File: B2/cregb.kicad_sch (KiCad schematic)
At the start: 9 parts, among them U105 74HC244, U108 74HC32, U110 74HC04, U115 74HC74, U120 74HC74, U124 74HC00, U125 74HC74, U127 74HC08, U128 74HC377

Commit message: B2 almost ready
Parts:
- removed U115, U120: 74HC74, Package_SO:SO-14_3.9x8.65mm_P1.27mm, symbol 74xx:74HC74
- added U316, U999: 74HC74, Package_SO:SO-14_3.9x8.65mm_P1.27mm, symbol 74xx:74HC74
- renumbered U105 to U205, U110 to U302, U124 to U303, U108 to U304, U128 to U305, U127 to U306, U125 to U308
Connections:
- net PHI2: now also U316.11 (C), U999.11 (C)
- net VCC: now also U316.10 (~{S}), U316.13 (~{R}), U999.1 (~{R}), U999.10 (~{S}), U999.13 (~{R}), U999.4 (~{S})
- net ~{PHI2}: now also U999.3 (C)
- net TBRUNMODE: now reaches U304.10
- net TBRUNMODE: now also U205.15 (2A1), U305.12 (Q4), U316.12 (D)
- net at U308.9 (Q): now also U999.12 (D)
- net PB6ON renamed PB7ON
- net SPMODE renamed TBINMODE1
- net TAINMODE renamed TBINMODE0
- net TAOUTMODE renamed TBOUTMODE
- removed net TARUNMODE: U205.15 (2A1), U304.9, U305.12 (Q4)
- net TAUNDERFLOW renamed TBUNDERFLOW
- net TODIN renamed ALARM
- net rTASTART renamed rTBSTART
- net rTBSTART: now also U999.2 (D)
- net ~{EN14} renamed ~{EN15}
- new net: U304.9, U316.9 (Q)
- new net TBLOAD: U999.9 (Q)
- new net TBSTART: U999.5 (Q)
- new net ~{TBSTART}: U999.6 (~{Q})
- no-connect marks 7 -> 6
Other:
- moved on the sheet: U304C

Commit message: Almost 0.1.1
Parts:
- renumbered U304 to U208, U302 to U210, U316 to U213, U999 to U222, U308 to U223, U303 to U227, U305 to U228, U306 to U229
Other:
- title: 74HCT6526 Board 1 -> 74HCT6526 Board 2
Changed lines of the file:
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@@
   (paper "A4")
   (title_block
-    (title "74HCT6526 Board 1")
-    (date "2022-03-20")
-    (rev "0.0")
+    (title "74HCT6526 Board 2")
+    (date "2022-08-17")
+    (rev "0.1")
     (company "Daniel Molina")
     (comment 1 "https://github.com/dmolinagarcia/74HCT6526")
@@
   (symbol (lib_id "74xx:74HC04") (at 87.63 102.87 0) (unit 5)
     (in_bom yes) (on_board yes)
-    (property "Reference" "U302" (id 0) (at 86.995 102.87 0))
+    (property "Reference" "U210" (id 0) (at 86.995 102.87 0))
     (property "Value" "74HC04" (id 1) (at 87.63 97.8686 0))
     (property "Footprint" "Package_SO:SOIC-14_3.9x8.7mm_P1.27mm" (id 2) (at 87.63 102.87 0)
@@
   (symbol (lib_id "74xx:74HC00") (at 50.8 68.58 0) (unit 1)
     (in_bom yes) (on_board yes)
-    (property "Reference" "U303" (id 0) (at 50.8 68.58 0))
+    (property "Reference" "U227" (id 0) (at 50.8 68.58 0))
     (property "Value" "74HC00" (id 1) (at 50.8 74.93 0))
     (property "Footprint" "Package_SO:SOIC-14_3.9x8.7mm_P1.27mm" (id 2) (at 50.8 68.58 0)
@@
   (symbol (lib_id "74xx:74HC74") (at 127 116.84 0) (unit 2)
     (in_bom yes) (on_board yes) (fields_autoplaced)
-    (property "Reference" "U316" (id 0) (at 129.0194 107.7935 0)
+    (property "Reference" "U213" (id 0) (at 129.0194 107.7935 0)
       (effects (font (size 1.27 1.27)) (justify left))
     )
@@
   (symbol (lib_id "74xx:74LS32") (at 153.67 116.84 0) (unit 3)
     (in_bom yes) (on_board yes)
-    (property "Reference" "U304" (id 0) (at 153.67 116.84 0))
+    (property "Reference" "U208" (id 0) (at 153.67 116.84 0))
     (property "Value" "74HC32" (id 1) (at 153.035 122.555 0))
     (property "Footprint" "Package_SO:SOIC-14_3.9x8.7mm_P1.27mm" (id 2) (at 153.67 116.84 0)
@@
   (symbol (lib_id "74xx:74HC00") (at 171.45 119.38 0) (unit 2)
     (in_bom yes) (on_board yes)
-    (property "Reference" "U303" (id 0) (at 171.45 119.38 0))
+    (property "Reference" "U227" (id 0) (at 171.45 119.38 0))
     (property "Value" "74HC00" (id 1) (at 171.45 114.3786 0))
     (property "Footprint" "Package_SO:SOIC-14_3.9x8.7mm_P1.27mm" (id 2) (at 171.45 119.38 0)
@@
   (symbol (lib_id "74xx:74HC74") (at 127 142.24 0) (unit 2)
     (in_bom yes) (on_board yes)
-    (property "Reference" "U308" (id 0) (at 126.365 142.24 0)
+    (property "Reference" "U223" (id 0) (at 126.365 142.24 0)
       (effects (font (size 1.27 1.27)) (justify left))
     )
@@
   (symbol (lib_id "74xx:74HC74") (at 160.02 142.24 0) (unit 2)
     (in_bom yes) (on_board yes)
-    (property "Reference" "U999" (id 0) (at 158.75 143.51 0)
+    (property "Reference" "U222" (id 0) (at 158.75 143.51 0)
       (effects (font (size 1.27 1.27)) (justify left))
     )
@@
   (symbol (lib_id "74xx:74HC74") (at 226.06 110.49 0) (unit 1)
     (in_bom yes) (on_board yes)
-    (property "Reference" "U999" (id 0) (at 224.79 110.49 0)
+    (property "Reference" "U222" (id 0) (at 224.79 110.49 0)
       (effects (font (size 1.27 1.27)) (justify left))
     )
@@
   (symbol (lib_id "74xx:74HC74") (at 180.34 95.25 0) (unit 1)
     (in_bom yes) (on_board yes)
-    (property "Reference" "U308" (id 0) (at 179.07 95.25 0)
+    (property "Reference" "U223" (id 0) (at 179.07 95.25 0)
       (effects (font (size 1.27 1.27)) (justify left))
     )
@@
   (symbol (lib_id "Custom 74xx:74HC08") (at 107.95 105.41 0) (unit 1)
     (in_bom yes) (on_board yes)
-    (property "Reference" "U306" (id 0) (at 107.315 105.41 0))
+    (property "Reference" "U229" (id 0) (at 107.315 105.41 0))
     (property "Value" "74HC08" (id 1) (at 107.95 100.4086 0))
     (property "Footprint" "Package_SO:SO-14_3.9x8.65mm_P1.27mm" (id 2) (at 107.95 105.41 0)
@@
   (symbol (lib_id "74xx:74LS32") (at 55.88 80.01 0) (unit 4)
     (in_bom yes) (on_board yes)
-    (property "Reference" "U304" (id 0) (at 55.88 80.01 0))
+    (property "Reference" "U208" (id 0) (at 55.88 80.01 0))
     (property "Value" "74HC32" (id 1) (at 55.88 85.09 0))
     (property "Footprint" "Package_SO:SOIC-14_3.9x8.7mm_P1.27mm" (id 2) (at 55.88 80.01 0)
@@
   (symbol (lib_id "74xx:74LS377") (at 100.33 46.99 0) (unit 1)
     (in_bom yes) (on_board yes) (fields_autoplaced)
-    (property "Reference" "U305" (id 0) (at 102.3494 27.7835 0)
+    (property "Reference" "U228" (id 0) (at 102.3494 27.7835 0)
       (effects (font (size 1.27 1.27)) (justify left))
     )
@@
   (symbol (lib_id "74xx:74HC00") (at 67.31 66.04 0) (unit 4)
     (in_bom yes) (on_board yes)
-    (property "Reference" "U303" (id 0) (at 67.31 66.04 0))
+    (property "Reference" "U227" (id 0) (at 67.31 66.04 0))
     (property "Value" "74HC00" (id 1) (at 67.31 71.12 0))
     (property "Footprint" "Package_SO:SOIC-14_3.9x8.7mm_P1.27mm" (id 2) (at 67.31 66.04 0)

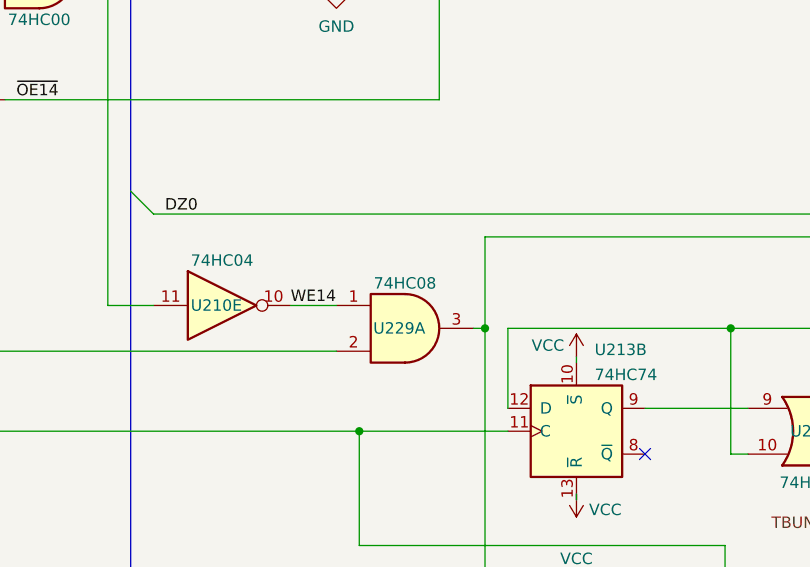
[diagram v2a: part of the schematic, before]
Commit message: Added ICR. B2 fixes
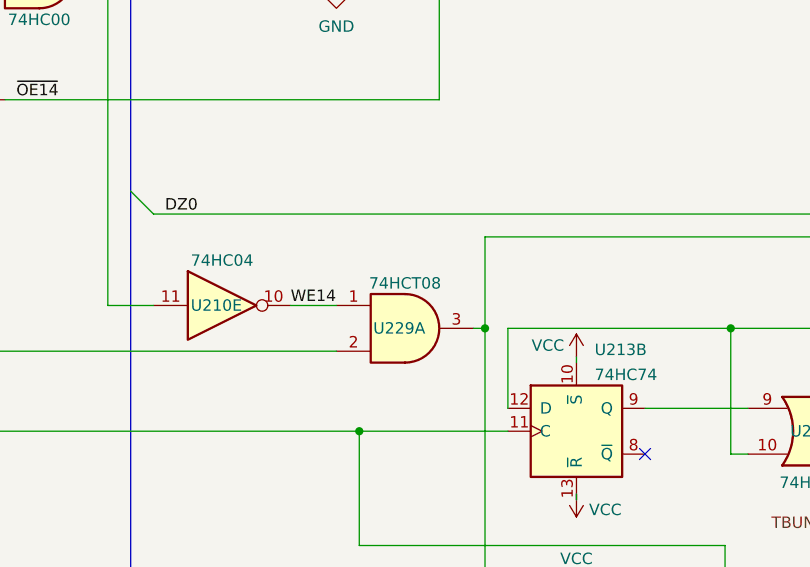
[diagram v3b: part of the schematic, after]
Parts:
- U229: value 74HC08 -> 74HCT08
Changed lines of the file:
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@@
     (in_bom yes) (on_board yes)
     (property "Reference" "U229" (id 0) (at 107.315 105.41 0))
-    (property "Value" "74HC08" (id 1) (at 107.95 100.4086 0))
+    (property "Value" "74HCT08" (id 1) (at 107.95 100.4086 0))
     (property "Footprint" "Package_SO:SO-14_3.9x8.65mm_P1.27mm" (id 2) (at 107.95 105.41 0)
       (effects (font (size 1.27 1.27)) hide)

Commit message: B0 ready for v0.2.0 release.
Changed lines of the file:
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@@
   (title_block
     (title "74HCT6526 Board 2")
-    (date "2022-10-08")
-    (rev "0.1.2")
+    (date "2023-01-22")
+    (rev "0.2.0")
     (company "Daniel Molina")
     (comment 1 "https://github.com/dmolinagarcia/74HCT6526")
@@
     (stroke (width 0) (type default) (color 0 0 0 0))
   )
+  (wire (pts (xy 229.87 25.4) (xy 229.87 26.67))
+    (stroke (width 0) (type default) (color 0 0 0 0))
+  )
   (wire (pts (xy 198.12 52.07) (xy 217.17 52.07))
     (stroke (width 0) (type default) (color 0 0 0 0))
@@
   )
   (wire (pts (xy 242.57 36.83) (xy 248.285 36.83))
+    (stroke (width 0) (type default) (color 0 0 0 0))
+  )
+  (wire (pts (xy 229.87 68.58) (xy 229.87 67.31))
     (stroke (width 0) (type default) (color 0 0 0 0))
   )
@@
     (pin "1")
   )
-  (symbol (lib_id "power:GND") (at 229.87 67.31 0) (unit 1)
-    (in_bom yes) (on_board yes) (fields_autoplaced)
-    (property "Reference" "#PWR0106" (id 0) (at 229.87 73.66 0)
-      (effects (font (size 1.27 1.27)) hide)
-    )
-    (property "Value" "GND" (id 1) (at 229.87 72.39 0))
-    (property "Footprint" "" (id 2) (at 229.87 67.31 0)
-      (effects (font (size 1.27 1.27)) hide)
-    )
-    (property "Datasheet" "" (id 3) (at 229.87 67.31 0)
+  (symbol (lib_id "power:GND") (at 229.87 68.58 0) (unit 1)
+    (in_bom yes) (on_board yes) (fields_autoplaced)
+    (property "Reference" "#PWR0106" (id 0) (at 229.87 74.93 0)
+      (effects (font (size 1.27 1.27)) hide)
+    )
+    (property "Value" "GND" (id 1) (at 229.87 73.66 0))
+    (property "Footprint" "" (id 2) (at 229.87 68.58 0)
+      (effects (font (size 1.27 1.27)) hide)
+    )
+    (property "Datasheet" "" (id 3) (at 229.87 68.58 0)
       (effects (font (size 1.27 1.27)) hide)
     )
@@
     (pin "1")
   )
-  (symbol (lib_id "power:VCC") (at 229.87 26.67 0) (unit 1)
-    (in_bom yes) (on_board yes) (fields_autoplaced)
-    (property "Reference" "#PWR0316" (id 0) (at 229.87 30.48 0)
-      (effects (font (size 1.27 1.27)) hide)
-    )
-    (property "Value" "VCC" (id 1) (at 229.87 23.0655 0))
-    (property "Footprint" "" (id 2) (at 229.87 26.67 0)
-      (effects (font (size 1.27 1.27)) hide)
-    )
-    (property "Datasheet" "" (id 3) (at 229.87 26.67 0)
-      (effects (font (size 1.27 1.27)) hide)
-    )
+  (symbol (lib_id "power:VCC") (at 229.87 25.4 0) (unit 1)
+    (in_bom yes) (on_board yes) (fields_autoplaced)
+    (property "Reference" "#PWR0316" (id 0) (at 229.87 29.21 0)
+      (effects (font (size 1.27 1.27)) hide)
+    )
+    (property "Value" "VCC" (id 1) (at 229.87 21.7955 0))
+    (property "Footprint" "" (id 2) (at 229.87 25.4 0)
+      (effects (font (size 1.27 1.27)) hide)
+    )
+    (property "Datasheet" "" (id 3) (at 229.87 25.4 0)
+      (effects (font (size 1.27 1.27)) hide)
+    )
